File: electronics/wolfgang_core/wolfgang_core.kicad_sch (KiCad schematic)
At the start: 0 parts

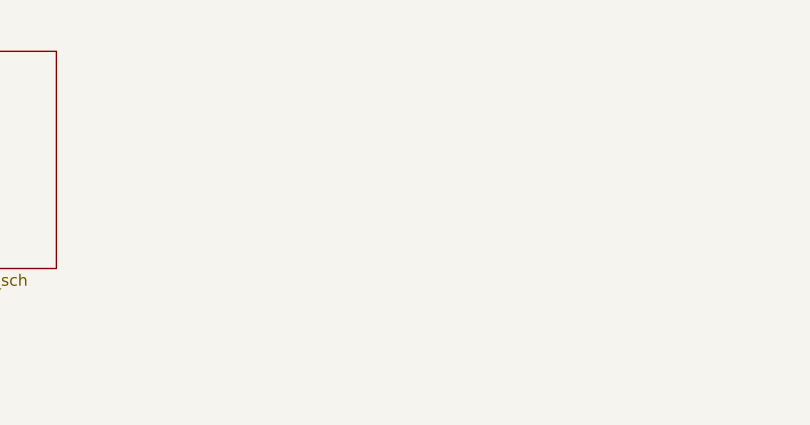
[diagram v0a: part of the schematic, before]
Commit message: Initial version USB to RS485
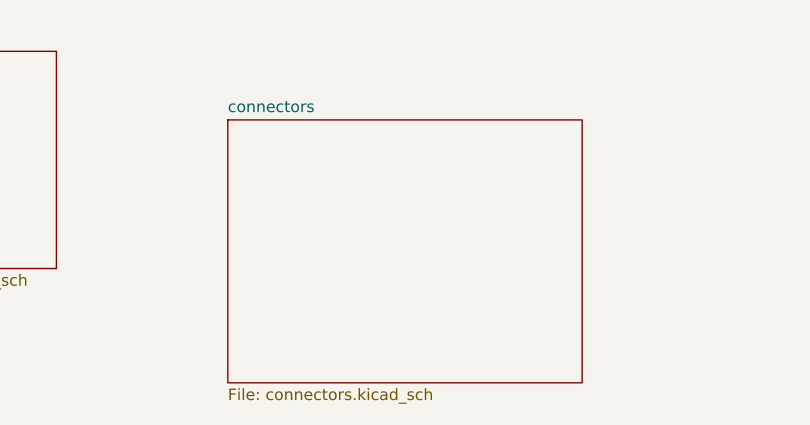
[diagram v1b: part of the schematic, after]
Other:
- added sheet connectors (connectors.kicad_sch)
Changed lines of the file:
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@@
-(kicad_sch (version 20211123) (generator eeschema)
+(kicad_sch (version 20230121) (generator eeschema)
   (paper "A4")
   (text "TODOs:\nRS485 Stuff:\n	FT4232H Module -> Chip only\n	Check Bus numbering with FTDI chip\nPower:\n	Softstart Mosfet\n	delete 9V\n	appropriately sized 5V converter\n	Check capacity requirements\n	priotitzied power path\n	fix sensing switch bodge"
@@
     (effects (font (size 1.27 1.27)) (justify left bottom))
   )
-  (sheet (at 57.15 40.64) (size 27.94 24.13) (fields_autoplaced)
-    (stroke (width 0.1524) (type solid) (color 0 0 0 0))
+  (sheet (at 104.14 48.26) (size 39.37 29.21) (fields_autoplaced)
+    (stroke (width 0.1524) (type solid))
     (fill (color 0 0 0 0.0000))
-    (property "Sheet name" "USB to RS485" (id 0) (at 57.15 39.9284 0)
+    (property "Sheetname" "connectors" (at 104.14 47.5484 0)
       (effects (font (size 1.27 1.27)) (justify left bottom))
     )
-    (property "Sheet file" "usb_to_rs485.kicad_sch" (id 1) (at 57.15 65.3546 0)
+    (property "Sheetfile" "connectors.kicad_sch" (at 104.14 78.0546 0)
       (effects (font (size 1.27 1.27)) (justify left top))
+    )
+    (instances
+      (project "wolfgang_core"
+        (path "/9538e4ed-27e6-4c37-b989-9859dc0d49e8" (page "3"))
+      )
+    )
+  )
+  (sheet (at 57.15 40.64) (size 27.94 24.13) (fields_autoplaced)
+    (stroke (width 0.1524) (type solid))
+    (fill (color 0 0 0 0.0000))
+    (property "Sheetname" "USB to RS485" (at 57.15 39.9284 0)
+      (effects (font (size 1.27 1.27)) (justify left bottom))
+    )
+    (property "Sheetfile" "usb_to_rs485.kicad_sch" (at 57.15 65.3546 0)
+      (effects (font (size 1.27 1.27)) (justify left top))
+    )
+    (instances
+      (project "wolfgang_core"
+        (path "/9538e4ed-27e6-4c37-b989-9859dc0d49e8" (page "2"))
+      )
     )
   )
   (sheet_instances
     (path "/" (page "1"))
-    (path "/e79c8e11-ed47-4701-ae80-a54cdb6682a5" (page "2"))
-  )
-  (symbol_instances
-    (path "/e79c8e11-ed47-4701-ae80-a54cdb6682a5/4fe60c97-cec9-4f03-ab68-167e75f325df"
-      (reference "#PWR?") (unit 1) (value "GND") (footprint "")
-    )
-    (path "/e79c8e11-ed47-4701-ae80-a54cdb6682a5/7500a369-c227-4fff-a7df-814253c07d86"
-      (reference "#PWR?") (unit 1) (value "GND") (footprint "")
-    )
-    (path "/e79c8e11-ed47-4701-ae80-a54cdb6682a5/ebc1216d-effe-4360-9e4b-17ef16121043"
-      (reference "#PWR?") (unit 1) (value "+5V") (footprint "")
-    )
-    (path "/e79c8e11-ed47-4701-ae80-a54cdb6682a5/14bf0b6b-dd4b-4c5f-bd2d-56881754b845"
-      (reference "C?") (unit 1) (value "0.1uF") (footprint "")
-    )
-    (path "/e79c8e11-ed47-4701-ae80-a54cdb6682a5/263a7eac-f1ba-4c92-849c-0efacd7a27ec"
-      (reference "C?") (unit 1) (value "0.1uF") (footprint "")
-    )
-    (path "/e79c8e11-ed47-4701-ae80-a54cdb6682a5/7dba6c2d-ae60-4529-9ae7-5aae597ce815"
-      (reference "C?") (unit 1) (value "0.1uF") (footprint "")
-    )
-    (path "/e79c8e11-ed47-4701-ae80-a54cdb6682a5/da356a1a-2b58-428d-a1a5-51a21e7d87a3"
-      (reference "C?") (unit 1) (value "0.1uF") (footprint "")
-    )
-    (path "/e79c8e11-ed47-4701-ae80-a54cdb6682a5/386d13b5-3a15-48e0-abd4-a201beb5cd69"
-      (reference "U?") (unit 1) (value "SP485ECN-L") (footprint "")
-    )
-    (path "/e79c8e11-ed47-4701-ae80-a54cdb6682a5/460d4342-da1e-4fd0-a971-759c60211659"
-      (reference "U?") (unit 1) (value "SP485ECN-L") (footprint "")
-    )
-    (path "/e79c8e11-ed47-4701-ae80-a54cdb6682a5/8a01f664-a9db-40d1-8745-89f74b069e18"
-      (reference "U?") (unit 1) (value "SP485ECN-L") (footprint "")
-    )
-    (path "/e79c8e11-ed47-4701-ae80-a54cdb6682a5/93c3af21-b55d-48d7-8765-064dd08a2bab"
-      (reference "U?") (unit 1) (value "FT4232H") (footprint "")
-    )
-    (path "/e79c8e11-ed47-4701-ae80-a54cdb6682a5/cdd9ecd7-ced4-4db8-87f6-e4d2a850d141"
-      (reference "U?") (unit 1) (value "SP485ECN-L") (footprint "")
-    )
-    (path "/e79c8e11-ed47-4701-ae80-a54cdb6682a5/470b3415-5ab9-4ca6-ad80-b7184fa90738"
-      (reference "Y?") (unit 1) (value "12MHz") (footprint "")
-    )
   )
 )

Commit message: Power largely done
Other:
- added sheet PoE Power Sourcing Equipment (PSE) (poe.kicad_sch)
- added sheet power (power.kicad_sch)
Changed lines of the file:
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@@
     (effects (font (size 1.27 1.27)) (justify left bottom))
+  )
+  (sheet (at 58.42 91.44) (size 39.37 29.21) (fields_autoplaced)
+    (stroke (width 0.1524) (type solid))
+    (fill (color 0 0 0 0.0000))
+    (property "Sheetname" "power" (at 58.42 90.7284 0)
+      (effects (font (size 1.27 1.27)) (justify left bottom))
+    )
+    (property "Sheetfile" "power.kicad_sch" (at 58.42 121.2346 0)
+      (effects (font (size 1.27 1.27)) (justify left top))
+    )
+    (instances
+      (project "wolfgang_core"
+        (path "/9538e4ed-27e6-4c37-b989-9859dc0d49e8" (page "4"))
+      )
+    )
+  )
+  (sheet (at 104.14 87.63) (size 53.34 38.1) (fields_autoplaced)
+    (stroke (width 0.1524) (type solid))
+    (fill (color 0 0 0 0.0000))
+    (property "Sheetname" "PoE Power Sourcing Equipment (PSE)" (at 104.14 86.9184 0)
+      (effects (font (size 1.27 1.27)) (justify left bottom))
+    )
+    (property "Sheetfile" "poe.kicad_sch" (at 104.14 126.3146 0)
+      (effects (font (size 1.27 1.27)) (justify left top))
+    )
+    (instances
+      (project "wolfgang_core"
+        (path "/9538e4ed-27e6-4c37-b989-9859dc0d49e8" (page "5"))
+      )
+    )
   )
   (sheet (at 104.14 48.26) (size 39.37 29.21) (fields_autoplaced)

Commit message: more io stuff
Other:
- added sheet io (io.kicad_sch)
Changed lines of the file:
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@@
+    )
+  )
+  (sheet (at 157.48 46.99) (size 27.94 17.78) (fields_autoplaced)
+    (stroke (width 0.1524) (type solid))
+    (fill (color 0 0 0 0.0000))
+    (property "Sheetname" "io" (at 157.48 46.2784 0)
+      (effects (font (size 1.27 1.27)) (justify left bottom))
+    )
+    (property "Sheetfile" "io.kicad_sch" (at 157.48 65.3546 0)
+      (effects (font (size 1.27 1.27)) (justify left top))
+    )
+    (instances
+      (project "wolfgang_core"
+        (path "/9538e4ed-27e6-4c37-b989-9859dc0d49e8" (page "6"))
+      )
     )
   )
